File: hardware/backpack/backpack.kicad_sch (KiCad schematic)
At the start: 20 parts, among them J2 Conn_02x06_Top_Bottom, J3 Conn_02x06_Top_Bottom, J7 USB_C, J8 MICROMOD-2222, J9 USB_C

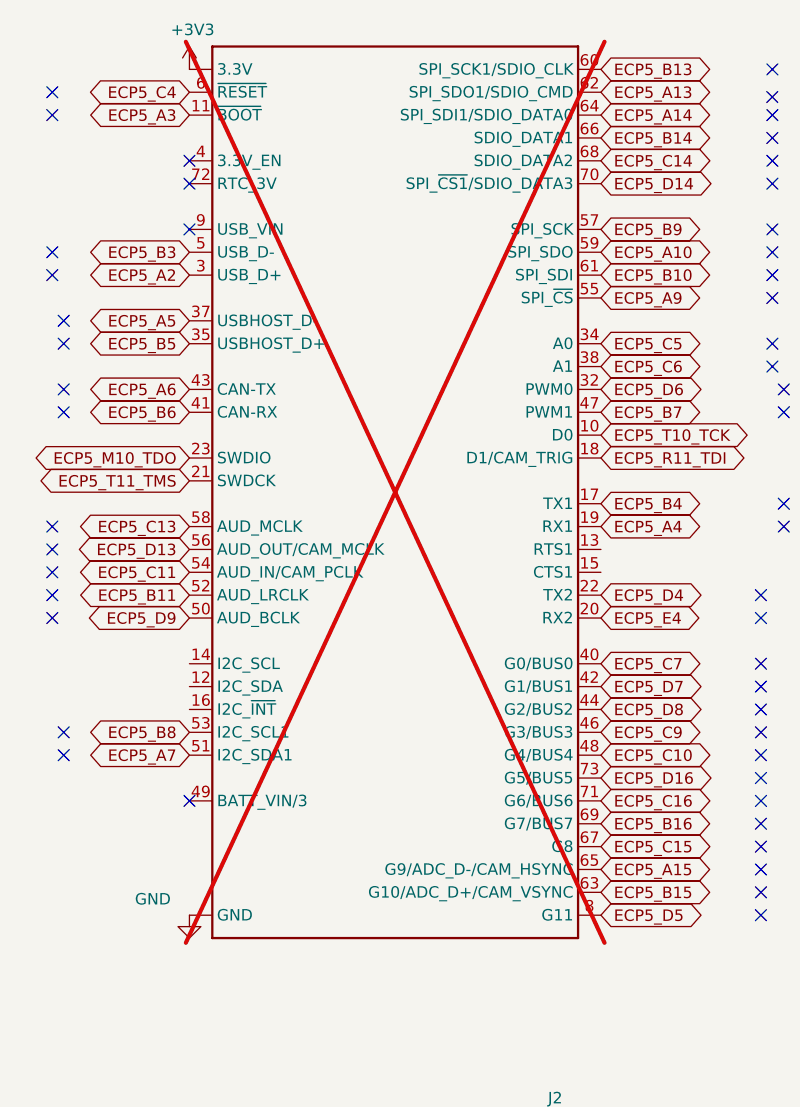
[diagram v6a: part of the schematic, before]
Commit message: tiliqua, m.2 footprint move/fix, lcsc# for m.2
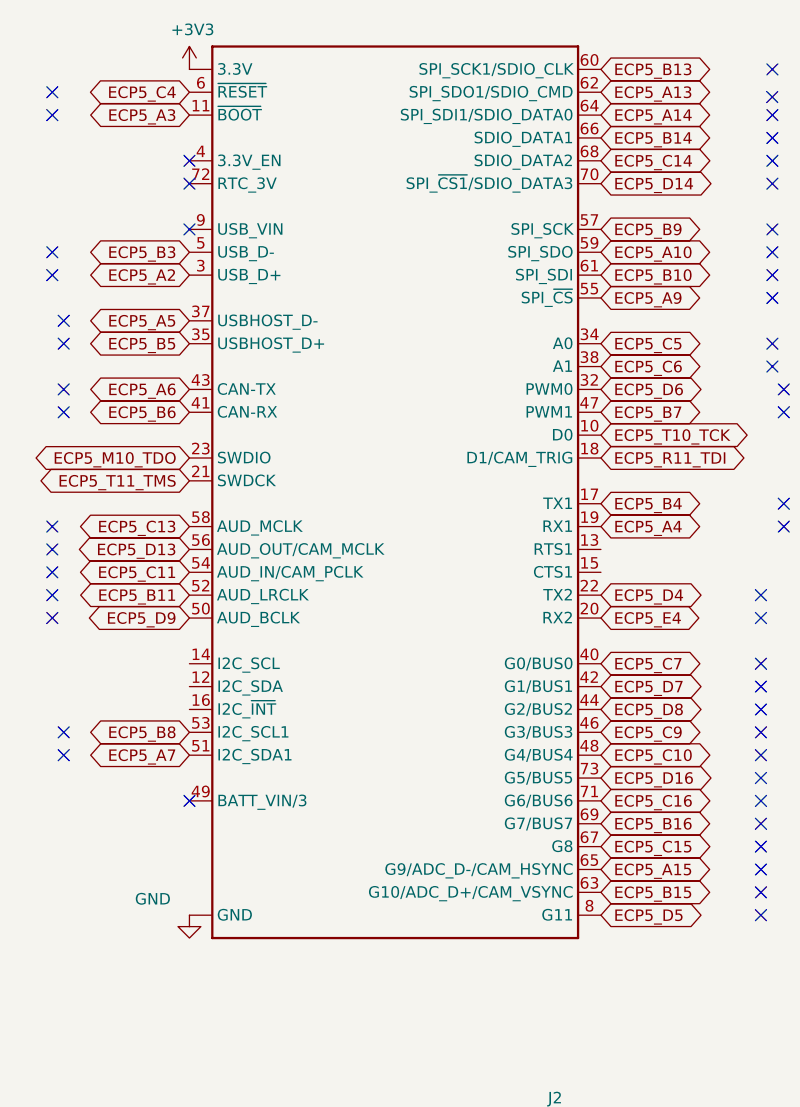
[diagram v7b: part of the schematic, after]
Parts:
- J8: lcsc# (none) -> C2977809; now fitted
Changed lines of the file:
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@@
 		(in_bom yes)
 		(on_board yes)
-		(dnp yes)
+		(dnp no)
 		(property "Reference" "J8"
 			(at 38.1 21.082 0)
@@
 			(at 58.42 74.93 0)
 			(effects
+				(font
+					(size 1.27 1.27)
+				)
+				(hide yes)
+			)
+		)
+		(property "lcsc#" "C2977809"
+			(at 58.42 74.93 0)
+			(effects

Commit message: updates before fab 04-04-24
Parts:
- C26: lcsc# C129131 -> C307331
- D4, D5: lcsc# C2840959 -> C493190
- R19, R20, R21, R22: value 5.1k -> 5.1K; lcsc# C105872 -> C25905
- R27: value 10k -> 10K; lcsc# C60490 -> C25744
- R29, R30: value 100R/R0402 -> 100R; lcsc# C106232 -> C25076
- SW1: value ~ -> SW_Tactile_SPST
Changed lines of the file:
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@@
 			)
 		)
-		(property "Value" "100R/R0402"
+		(property "Value" "100R"
 			(at 172.085 82.55 0)
 			(effects
@@
 			)
 		)
-		(property "Datasheet" ""
+		(property "Datasheet" "~"
 			(at 170.18 82.55 90)
 			(effects
@@
 			)
 		)
-		(property "lcsc#" "  C106232"
+		(property "lcsc#" "C25076"
 			(at 170.18 82.55 0)
 			(effects
@@
 			)
 		)
-		(property "Datasheet" ""
+		(property "Datasheet" "~"
 			(at 58.42 74.93 0)
 			(effects
@@
 			)
 		)
-		(property "Value" "100R/R0402"
+		(property "Value" "100R"
 			(at 165.735 82.55 0)
 			(effects
@@
 			)
 		)
-		(property "Datasheet" ""
+		(property "Datasheet" "~"
 			(at 163.83 82.55 90)
 			(effects
@@
 			)
 		)
-		(property "lcsc#" "  C106232"
+		(property "lcsc#" "C25076"
 			(at 163.83 82.55 0)
 			(effects
@@
 			)
 		)
-		(property "Value" "10k"
+		(property "Value" "10K"
 			(at 163.322 40.767 0)
 			(effects
@@
 			)
 		)
-		(property "lcsc#" "C60490"
+		(property "lcsc#" "C25744"
 			(at 165.1 41.91 0)
 			(effects
@@
 			)
 		)
-		(property "Value" "5.1k"
+		(property "Value" "5.1K"
 			(at 189.738 127 90)
 			(effects
@@
 			)
 		)
-		(property "lcsc#" "C105872"
+		(property "lcsc#" "C25905"
 			(at 191.77 127 0)
 			(effects
@@
 			)
 		)
-		(property "lcsc#" "C2840959"
+		(property "lcsc#" "C493190"
 			(at 46.99 184.15 0)
 			(effects
@@
 			)
 		)
-		(property "Datasheet" ""
+		(property "Datasheet" "~"
 			(at 156.21 134.62 0)
 			(effects
@@
 			)
 		)
-		(property "Value" "5.1k"
+		(property "Value" "5.1K"
 			(at 138.938 124.46 90)
 			(effects
@@
 			)
 		)
-		(property "lcsc#" "C105872"
+		(property "lcsc#" "C25905"
 			(at 140.97 124.46 0)
 			(effects
@@
 			)
 		)
-		(property "lcsc#" "C2840959"
+		(property "lcsc#" "C493190"
 			(at 46.99 180.34 0)
 			(effects
@@
 			)
 		)
-		(property "Datasheet" "~"
+		(property "Datasheet" ""
 			(at 165.1 54.61 0)
 			(effects
@@
 			)
 		)
-		(property "lcsc#" "C129131"
+		(property "lcsc#" " C307331"
 			(at 165.1 54.61 0)
 			(effects
@@
 			)
 		)
-		(property "Value" "5.1k"
+		(property "Value" "5.1K"
 			(at 138.938 127 90)
 			(effects
@@
 			)
 		)
-		(property "lcsc#" "C105872"
+		(property "lcsc#" "C25905"
 			(at 140.97 127 0)
 			(effects
@@
 			)
 		)
-		(property "Datasheet" ""
+		(property "Datasheet" "~"
 			(at 207.01 134.62 0)
 			(effects
@@
 			)
 		)
-		(property "Value" "~"
+		(property "Value" "SW_Tactile_SPST"
 			(at 173.99 46.99 0)
 			(effects
@@
 			)
 		)
-		(property "Value" "5.1k"
+		(property "Value" "5.1K"
 			(at 189.738 124.46 90)
 			(effects
@@
 			)
 		)
-		(property "lcsc#" "C105872"
+		(property "lcsc#" "C25905"
 			(at 191.77 124.46 0)
 			(effects
